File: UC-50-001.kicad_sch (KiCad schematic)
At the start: 0 parts

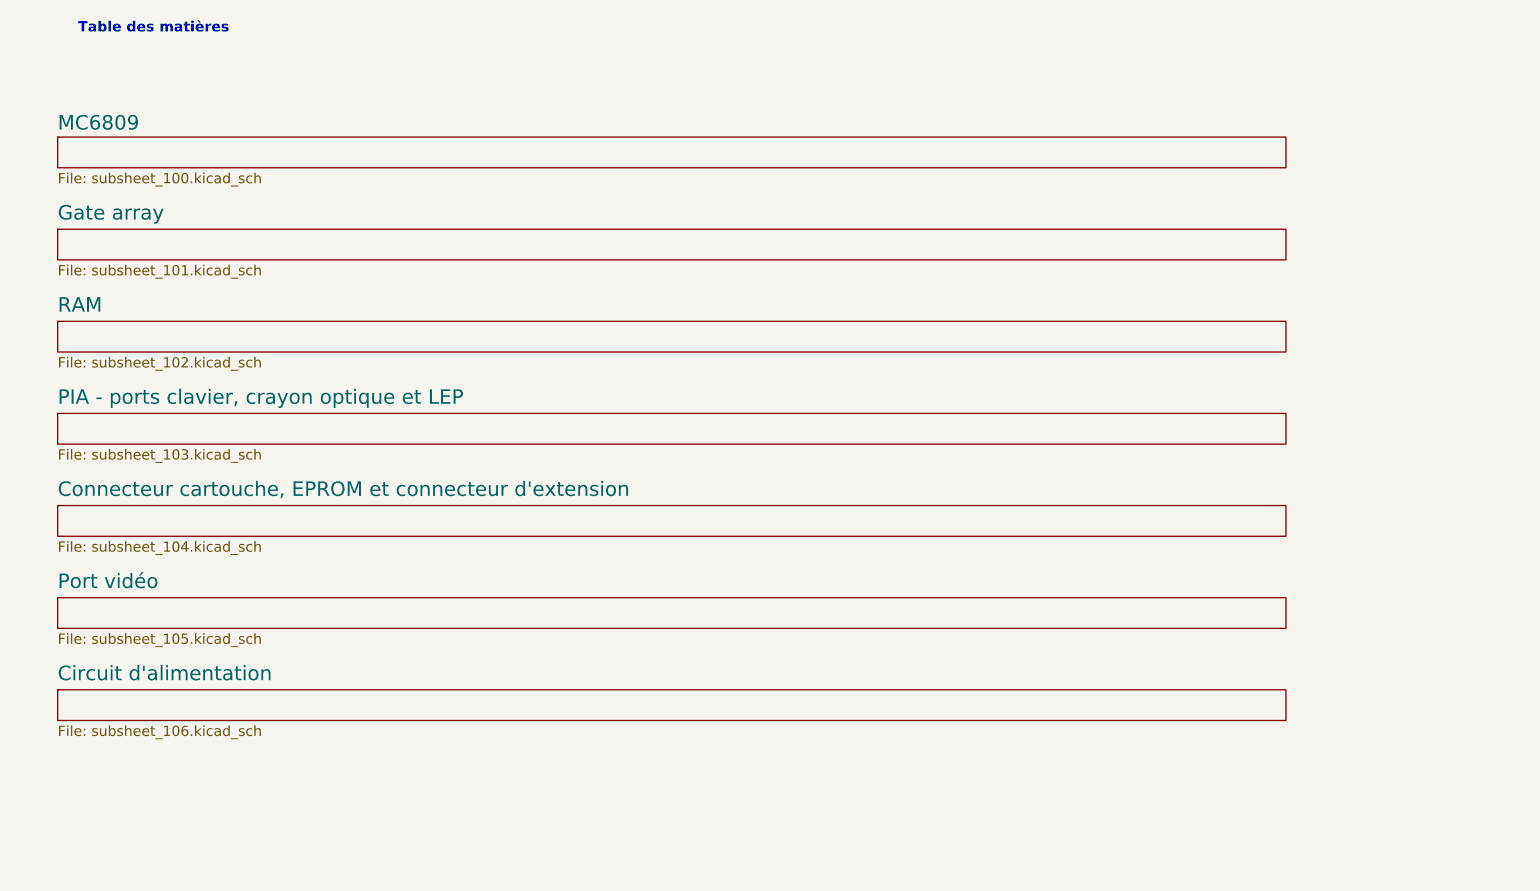
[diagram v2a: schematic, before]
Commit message: cpu : sépare le circuit reset du pull-up de la broche 34
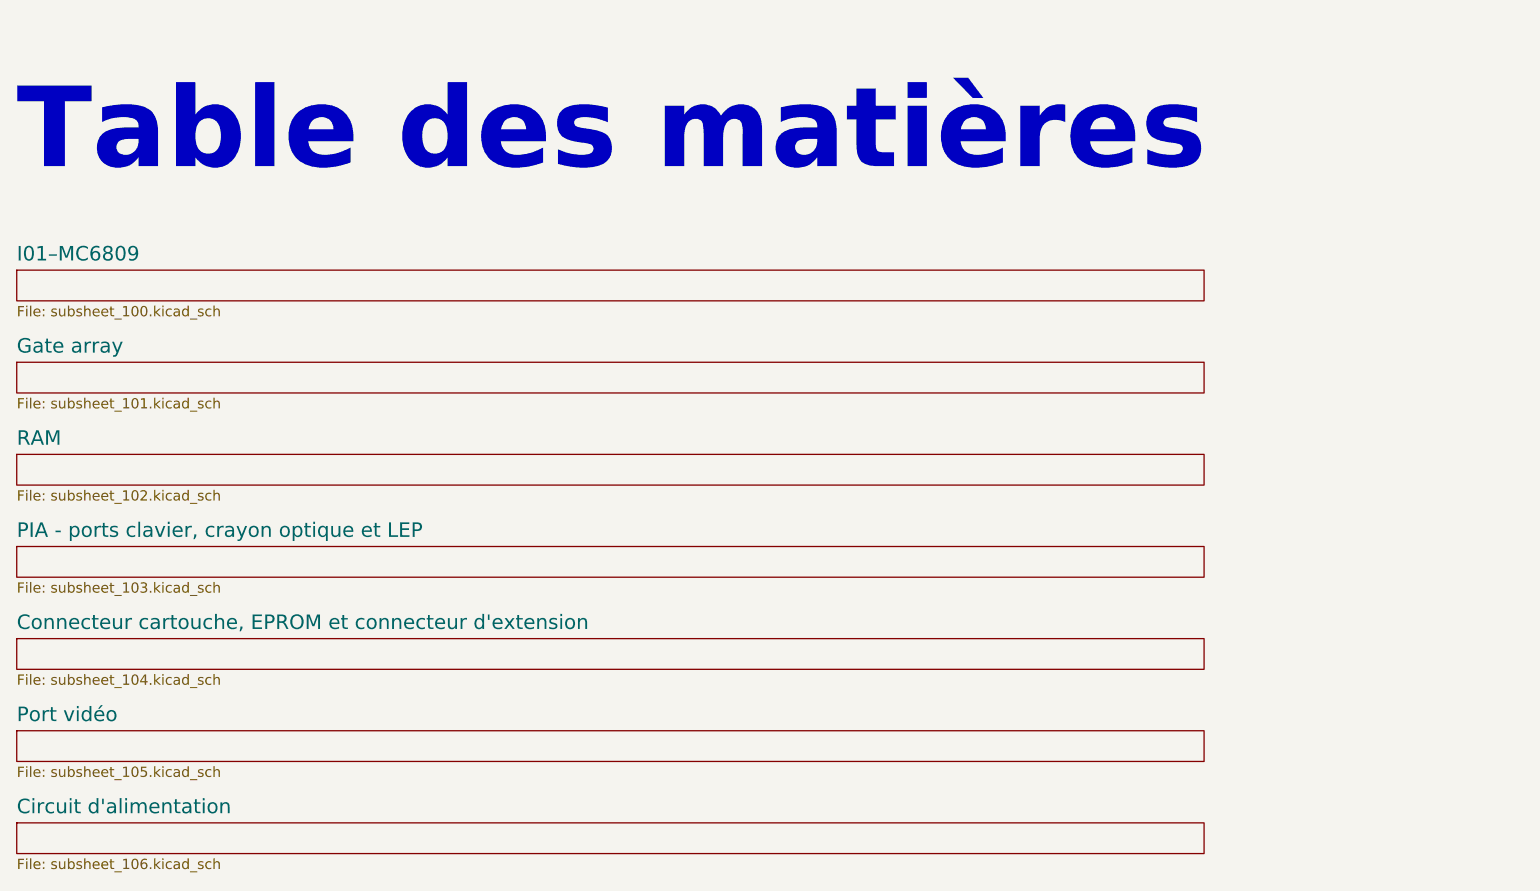
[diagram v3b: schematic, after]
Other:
- sheet MC6809 renamed I01–MC6809
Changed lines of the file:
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@@
     (rev "DRAFT")
   )
-  (text "Table des matières" (at 38.1 25.4 0)
-    (effects (font (size 1.27 1.27) (thickness 0.254) bold) (justify left bottom))
+  (text "Table des matières" (at 30.48 43.18 0)
+    (effects (font (size 10 10) (thickness 2.54) bold) (justify left bottom))
   )
-  (sheet (at 35.56 95.25) (size 152.4 3.81) (fields_autoplaced)
+  (sheet (at 30.48 111.76) (size 147.32 3.81) (fields_autoplaced)
     (stroke (width 0.1524) (type solid) (color 0 0 0 0))
     (fill (color 0 0 0 0.0000))
-    (property "Sheet name" "Port vidéo" (id 0) (at 35.56 94.2734 0)
+    (property "Sheet name" "Port vidéo" (id 0) (at 30.48 110.7834 0)
       (effects (font (size 1.8 1.8)) (justify left bottom))
     )
-    (property "Sheet file" "subsheet_105.kicad_sch" (id 1) (at 35.56 99.6446 0)
+    (property "Sheet file" "subsheet_105.kicad_sch" (id 1) (at 30.48 116.1546 0)
       (effects (font (size 1.27 1.27)) (justify left top))
     )
   )
-  (sheet (at 35.56 60.96) (size 152.4 3.81) (fields_autoplaced)
+  (sheet (at 30.48 77.47) (size 147.32 3.81) (fields_autoplaced)
     (stroke (width 0.1524) (type solid) (color 0 0 0 0))
     (fill (color 0 0 0 0.0000))
-    (property "Sheet name" "RAM" (id 0) (at 35.56 59.9834 0)
+    (property "Sheet name" "RAM" (id 0) (at 30.48 76.4934 0)
       (effects (font (size 1.8 1.8)) (justify left bottom))
     )
-    (property "Sheet file" "subsheet_102.kicad_sch" (id 1) (at 35.56 65.3546 0)
+    (property "Sheet file" "subsheet_102.kicad_sch" (id 1) (at 30.48 81.8646 0)
       (effects (font (size 1.27 1.27)) (justify left top))
     )
   )
-  (sheet (at 35.56 106.68) (size 152.4 3.81) (fields_autoplaced)
+  (sheet (at 30.48 123.19) (size 147.32 3.81) (fields_autoplaced)
     (stroke (width 0.1524) (type solid) (color 0 0 0 0))
     (fill (color 0 0 0 0.0000))
-    (property "Sheet name" "Circuit d'alimentation" (id 0) (at 35.56 105.7034 0)
+    (property "Sheet name" "Circuit d'alimentation" (id 0) (at 30.48 122.2134 0)
       (effects (font (size 1.8 1.8)) (justify left bottom))
     )
-    (property "Sheet file" "subsheet_106.kicad_sch" (id 1) (at 35.56 111.0746 0)
+    (property "Sheet file" "subsheet_106.kicad_sch" (id 1) (at 30.48 127.5846 0)
       (effects (font (size 1.27 1.27)) (justify left top))
     )
   )
-  (sheet (at 35.56 38.1) (size 152.4 3.81) (fields_autoplaced)
+  (sheet (at 30.48 54.61) (size 147.32 3.81) (fields_autoplaced)
     (stroke (width 0.1524) (type solid) (color 0 0 0 0))
     (fill (color 0 0 0 0.0000))
-    (property "Sheet name" "MC6809" (id 0) (at 35.56 37.3884 0)
+    (property "Sheet name" "I01–MC6809" (id 0) (at 30.48 53.6334 0)
       (effects (font (size 1.8 1.8)) (justify left bottom))
     )
-    (property "Sheet file" "subsheet_100.kicad_sch" (id 1) (at 35.56 42.4946 0)
+    (property "Sheet file" "subsheet_100.kicad_sch" (id 1) (at 30.48 59.0046 0)
       (effects (font (size 1.27 1.27)) (justify left top))
     )
   )
-  (sheet (at 35.56 72.39) (size 152.4 3.81) (fields_autoplaced)
+  (sheet (at 30.48 88.9) (size 147.32 3.81) (fields_autoplaced)
     (stroke (width 0.1524) (type solid) (color 0 0 0 0))
     (fill (color 0 0 0 0.0000))
-    (property "Sheet name" "PIA - ports clavier, crayon optique et LEP" (id 0) (at 35.56 71.4134 0)
+    (property "Sheet name" "PIA - ports clavier, crayon optique et LEP" (id 0) (at 30.48 87.9234 0)
       (effects (font (size 1.8 1.8)) (justify left bottom))
     )
-    (property "Sheet file" "subsheet_103.kicad_sch" (id 1) (at 35.56 76.7846 0)
+    (property "Sheet file" "subsheet_103.kicad_sch" (id 1) (at 30.48 93.2946 0)
       (effects (font (size 1.27 1.27)) (justify left top))
     )
   )
-  (sheet (at 35.56 83.82) (size 152.4 3.81) (fields_autoplaced)
+  (sheet (at 30.48 100.33) (size 147.32 3.81) (fields_autoplaced)
     (stroke (width 0.1524) (type solid) (color 0 0 0 0))
     (fill (color 0 0 0 0.0000))
-    (property "Sheet name" "Connecteur cartouche, EPROM et connecteur d'extension" (id 0) (at 35.56 82.8434 0)
+    (property "Sheet name" "Connecteur cartouche, EPROM et connecteur d'extension" (id 0) (at 30.48 99.3534 0)
       (effects (font (size 1.8 1.8)) (justify left bottom))
     )
-    (property "Sheet file" "subsheet_104.kicad_sch" (id 1) (at 35.56 88.2146 0)
+    (property "Sheet file" "subsheet_104.kicad_sch" (id 1) (at 30.48 104.7246 0)
       (effects (font (size 1.27 1.27)) (justify left top))
     )
   )
-  (sheet (at 35.56 49.53) (size 152.4 3.81) (fields_autoplaced)
+  (sheet (at 30.48 66.04) (size 147.32 3.81) (fields_autoplaced)
     (stroke (width 0.1524) (type solid) (color 0 0 0 0))
     (fill (color 0 0 0 0.0000))
-    (property "Sheet name" "Gate array" (id 0) (at 35.56 48.5534 0)
+    (property "Sheet name" "Gate array" (id 0) (at 30.48 65.0634 0)
       (effects (font (size 1.8 1.8)) (justify left bottom))
     )
-    (property "Sheet file" "subsheet_101.kicad_sch" (id 1) (at 35.56 53.9246 0)
+    (property "Sheet file" "subsheet_101.kicad_sch" (id 1) (at 30.48 70.4346 0)
       (effects (font (size 1.27 1.27)) (justify left top))
     )
@@
       (reference "#PWR?") (unit 1) (value "GND") (footprint "")
     )
+    (path "/afd59d07-bfd6-4bc9-8176-e0ddec1872a1/ff5980ac-3ed4-4d48-96ee-600ed1fc706b"
+      (reference "#PWR?") (unit 1) (value "+5V") (footprint "")
+    )
     (path "/afd59d07-bfd6-4bc9-8176-e0ddec1872a1/b1f3febb-cebe-447d-bd66-d33f45b30c3e"

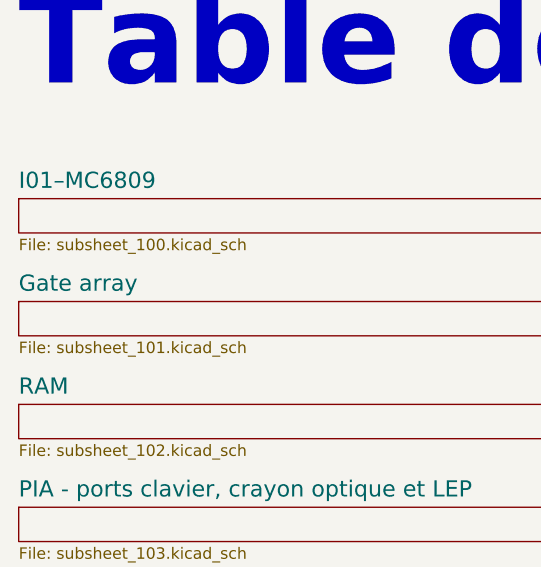
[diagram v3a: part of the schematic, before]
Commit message: information schéma, commence le gate array I29
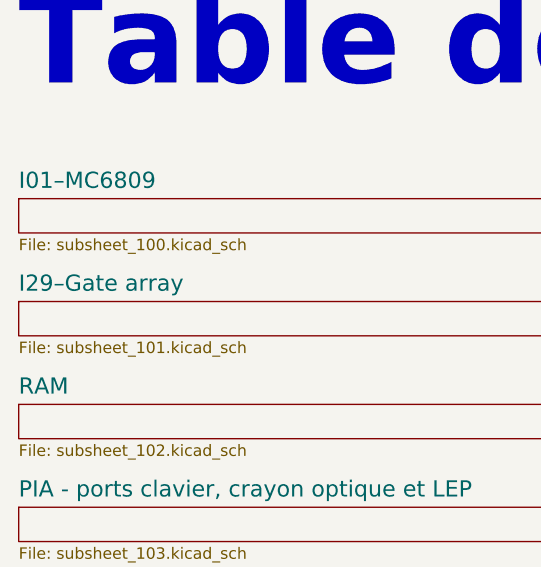
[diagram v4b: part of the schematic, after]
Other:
- sheet Gate array renamed I29–Gate array
- title: (none) -> Conversion du Thomson MO5 — Unité centrale
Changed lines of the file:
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@@
   (paper "A4" portrait)
   (title_block
+    (title "Conversion du Thomson MO5 — Unité centrale")
     (date "2023-05-12")
     (rev "DRAFT")
+    (comment 1 "http://github.com/sporniket/kicad-conversions--thomson-mo5--v1")
+    (comment 2 "Dépôt d'origine : ")
+    (comment 4 "Reference : POP5001 501994-01")
   )
   (text "Table des matières" (at 30.48 43.18 0)
@@
     (stroke (width 0.1524) (type solid) (color 0 0 0 0))
     (fill (color 0 0 0 0.0000))
-    (property "Sheet name" "Gate array" (id 0) (at 30.48 65.0634 0)
+    (property "Sheet name" "I29–Gate array" (id 0) (at 30.48 65.0634 0)
       (effects (font (size 1.8 1.8)) (justify left bottom))
     )
@@
       (reference "#FLG?") (unit 1) (value "PWR_FLAG") (footprint "")
     )
+    (path "/f465a4b1-7c3c-40cc-9e66-ff9f17003d42/0f6a8f7c-8ebc-48ff-a299-e91c43441b34"
+      (reference "#PWR?") (unit 1) (value "GND") (footprint "")
+    )
+    (path "/f465a4b1-7c3c-40cc-9e66-ff9f17003d42/15874553-68ab-458b-ae01-947d42d84e45"
+      (reference "#PWR?") (unit 1) (value "GND") (footprint "")
+    )
     (path "/afd59d07-bfd6-4bc9-8176-e0ddec1872a1/247a424e-59b0-4969-a300-9e89f564274f"
       (reference "#PWR?") (unit 1) (value "+5V") (footprint "")
     )
+    (path "/f465a4b1-7c3c-40cc-9e66-ff9f17003d42/2f8f66c7-e38d-418c-8487-2dbff27a54d9"
+      (reference "#PWR?") (unit 1) (value "+5V") (footprint "")
+    )
     (path "/afd59d07-bfd6-4bc9-8176-e0ddec1872a1/4b4eb77b-e691-46e0-83b1-1e19aba248f9"
       (reference "#PWR?") (unit 1) (value "+5V") (footprint "")
     )
+    (path "/f465a4b1-7c3c-40cc-9e66-ff9f17003d42/4ed64b04-c40d-47e3-8d56-edd00777bbe3"
+      (reference "#PWR?") (unit 1) (value "GND") (footprint "")
+    )
     (path "/afd59d07-bfd6-4bc9-8176-e0ddec1872a1/601e7756-9222-41ed-b96b-8651f8dceb01"
       (reference "#PWR?") (unit 1) (value "GND") (footprint "")
     )
+    (path "/f465a4b1-7c3c-40cc-9e66-ff9f17003d42/7448185d-14c9-4b5d-94f8-805bd81682bd"
+      (reference "#PWR?") (unit 1) (value "+5V") (footprint "")
+    )
     (path "/afd59d07-bfd6-4bc9-8176-e0ddec1872a1/76921501-701f-4c1f-8225-7bfdc888d467"
       (reference "#PWR?") (unit 1) (value "GND") (footprint "")
     )
+    (path "/f465a4b1-7c3c-40cc-9e66-ff9f17003d42/8621ba63-4cea-4096-85ae-020ac97482fe"
+      (reference "#PWR?") (unit 1) (value "GND") (footprint "")
+    )
+    (path "/f465a4b1-7c3c-40cc-9e66-ff9f17003d42/91b9ef3b-7eda-43c9-9d9b-33dfe0701bf3"
+      (reference "#PWR?") (unit 1) (value "+5V") (footprint "")
+    )
     (path "/afd59d07-bfd6-4bc9-8176-e0ddec1872a1/9b9e676b-a45e-44f0-8f14-e409b9618c02"
       (reference "#PWR?") (unit 1) (value "GND") (footprint "")
@@
       (reference "#PWR?") (unit 1) (value "GND") (footprint "")
     )
+    (path "/f465a4b1-7c3c-40cc-9e66-ff9f17003d42/ba7d33fe-5255-4475-a393-af7125edc5b0"
+      (reference "#PWR?") (unit 1) (value "+5V") (footprint "")
+    )
     (path "/706ec47c-3d4a-4bde-bb8b-c4f8dcc96c45/be048e59-199c-451b-9cb0-184def87f172"
       (reference "#PWR?") (unit 1) (value "+5V") (footprint "")
@@
     (path "/afd59d07-bfd6-4bc9-8176-e0ddec1872a1/d396128e-0019-4b81-b8de-65492819bfe3"
       (reference "#PWR?") (unit 1) (value "GND") (footprint "")
+    )
+    (path "/f465a4b1-7c3c-40cc-9e66-ff9f17003d42/de0c8acb-f7f4-46fa-b6df-ccef1391dc55"
+      (reference "#PWR?") (unit 1) (value "GND") (footprint "")
+    )
+    (path "/f465a4b1-7c3c-40cc-9e66-ff9f17003d42/e91d3ea8-c976-459f-bdce-4632596940fa"
+      (reference "#PWR?") (unit 1) (value "+5V") (footprint "")
     )
     (path "/afd59d07-bfd6-4bc9-8176-e0ddec1872a1/ff5980ac-3ed4-4d48-96ee-600ed1fc706b"
@@
       (reference "C21") (unit 1) (value "47nF") (footprint "")
     )
+    (path "/f465a4b1-7c3c-40cc-9e66-ff9f17003d42/6d589334-ed46-4724-8f6a-46e5f08827d1"
+      (reference "C37") (unit 1) (value "47nF") (footprint "")
+    )
+    (path "/f465a4b1-7c3c-40cc-9e66-ff9f17003d42/6fe8fa32-32ab-40d4-b1c2-f8724ff54f1f"
+      (reference "C?") (unit 1) (value "47nF") (footprint "")
+    )
+    (path "/f465a4b1-7c3c-40cc-9e66-ff9f17003d42/752990f8-3808-4a2b-97ee-454a291ef834"
+      (reference "C?") (unit 1) (value "100uF") (footprint "")
+    )
     (path "/afd59d07-bfd6-4bc9-8176-e0ddec1872a1/3cbb13a3-3bd9-42e8-a4d0-bff01ca1a44a"
       (reference "D01") (unit 1) (value "1N4148") (footprint "")
     )
+    (path "/f465a4b1-7c3c-40cc-9e66-ff9f17003d42/4aaf27b4-477d-4a41-877e-4da58d8db8c8"
+      (reference "D?") (unit 1) (value "1N4148") (footprint "")
+    )
     (path "/afd59d07-bfd6-4bc9-8176-e0ddec1872a1/63085d07-f111-48f0-9996-774660e796f0"
       (reference "I01") (unit 1) (value "MC6809EP") (footprint "Package_DIP:DIP-40_W15.24mm_LongPads")
     )
+    (path "/f465a4b1-7c3c-40cc-9e66-ff9f17003d42/2edb98bf-6c70-4551-a503-f7af487edfe6"
+      (reference "I29") (unit 1) (value "GATE_ARRAY_MO5_V1_PHY") (footprint "Package_LCC:PLCC-68_THT-Socket")
+    )
     (path "/b7e71b61-5858-491f-a12d-087d8cf2d648/d5845f7a-5010-4c58-a702-33af790aa3cb"
       (reference "I48") (unit 1) (value "PERIPHERAL_INTERFACE_ADAPTER_PHY") (footprint "Package_DIP:DIP-40_W15.24mm_LongPads")
@@
       (reference "R13") (unit 1) (value "3K3") (footprint "")
     )
+    (path "/f465a4b1-7c3c-40cc-9e66-ff9f17003d42/01bd2083-9983-4a62-a624-7879593e4acc"
+      (reference "R?") (unit 1) (value "3K3") (footprint "")
+    )
+    (path "/f465a4b1-7c3c-40cc-9e66-ff9f17003d42/e313687f-8819-4461-8d98-fbb47e818ae2"
+      (reference "R?") (unit 1) (value "1K") (footprint "")
+    )
     (path "/afd59d07-bfd6-4bc9-8176-e0ddec1872a1/d678cbcc-ae6f-420a-a5ee-0e01cba26e31"
       (reference "S01") (unit 1) (value "Initial Prog.") (footprint "")
@@
       (reference "U?") (unit 1) (value "16384-WORD_BY_4-BIT_DYNAMIC_RAM_PHY") (footprint "Package_DIP:DIP-18_W7.62mm_LongPads")
     )
-    (path "/f465a4b1-7c3c-40cc-9e66-ff9f17003d42/2edb98bf-6c70-4551-a503-f7af487edfe6"
-      (reference "U?") (unit 1) (value "GATE_ARRAY_MO5_V1_PHY") (footprint "Package_LCC:PLCC-68_THT-Socket")
-    )
     (path "/3b9df46e-3592-4470-9765-1c36c3c4b1c2/45f1b914-2512-4187-bc68-201a3ab3400f"
